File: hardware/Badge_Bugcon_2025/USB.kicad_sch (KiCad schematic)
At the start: 38 parts, among them J10 Battery, J3 USB_A, J4 USB_A, J6 USB_A, P4 USB_C_Plug_USB2.0, Q1 DMG3415U-7, SW1 ON, SW4 On, U1 USB3740B-AI9, U2 TP4056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

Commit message: feat(Hw):Update_Schematic_And_Floorplan
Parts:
- J10: footprint Footprints:Batt -> Battery:BatteryHolder_Keystone_1042_1x18650
- R31: footprint LED_SMD:LED_0603_1608Metric -> Resistor_SMD:R_0603_1608Metric
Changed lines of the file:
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@@
 			)
 		)
-		(property "Footprint" "Footprints:Batt"
+		(property "Footprint" "Battery:BatteryHolder_Keystone_1042_1x18650"
 			(at 274.32 60.96 0)
 			(effects
@@
 			)
 		)
-		(property "Footprint" "LED_SMD:LED_0603_1608Metric"
+		(property "Footprint" "Resistor_SMD:R_0603_1608Metric"
 			(at 184.912 57.15 90)
 			(effects

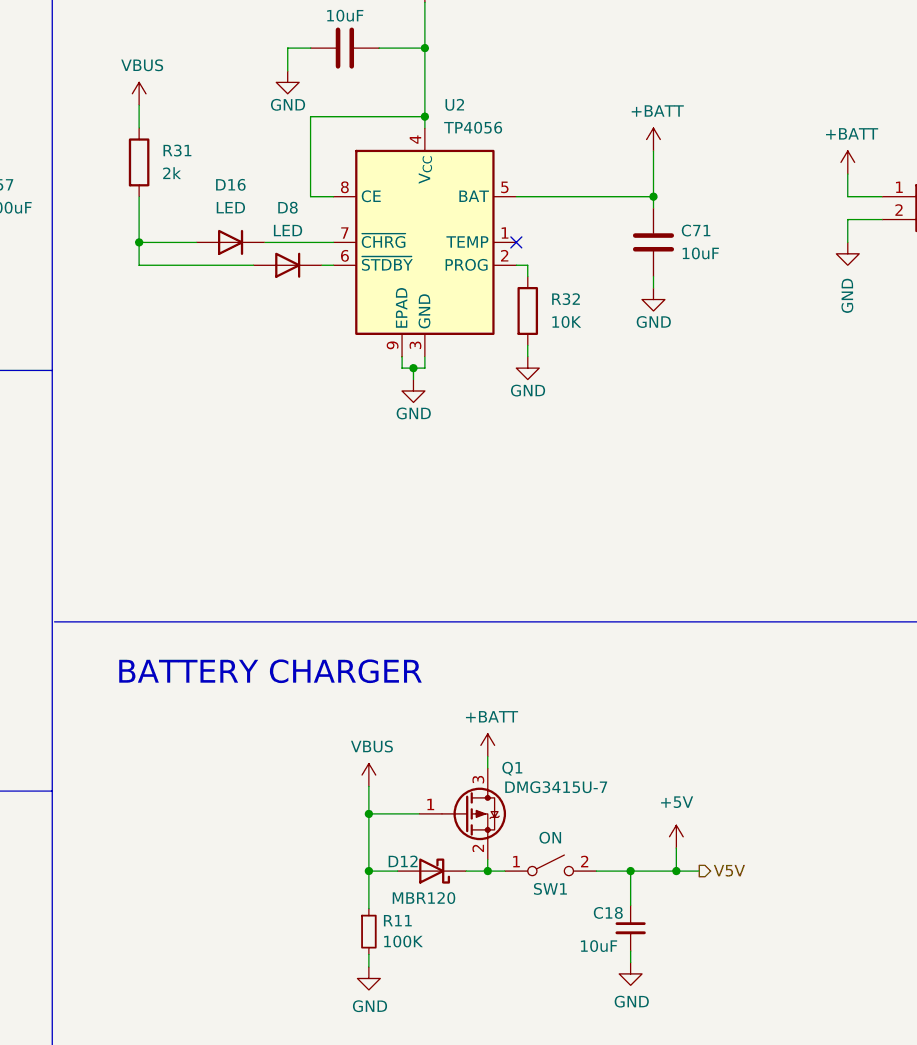
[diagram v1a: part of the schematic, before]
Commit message: feat(Hw):Update_Schematic_And_Floorplan
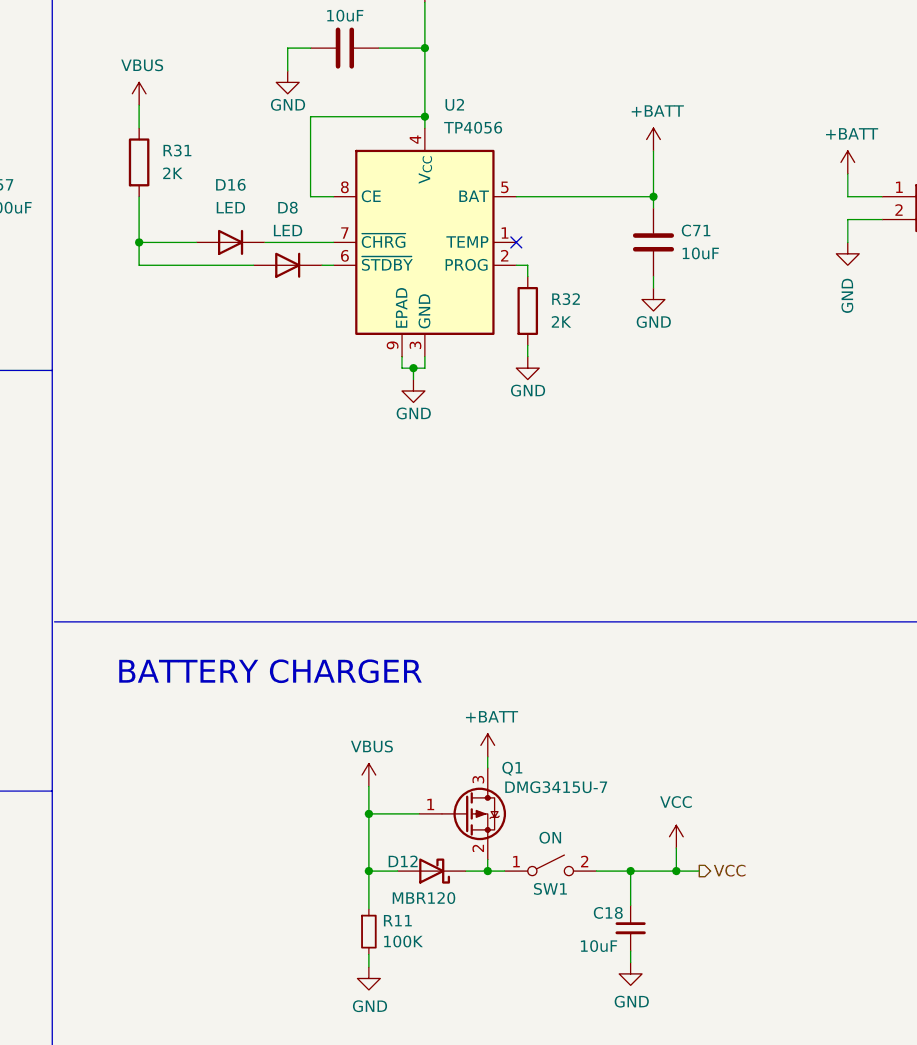
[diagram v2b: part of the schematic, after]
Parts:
- J10: footprint Battery:BatteryHolder_Keystone_1042_1x18650 -> Footprints:BatteryHolder_Keystone_1042_1x18650
- R31: value 2k -> 2K
- R32: value 10K -> 2K; footprint Resistor_SMD:R_0402_1005Metric -> Resistor_SMD:R_0603_1608Metric; LCSC# C2759535 -> C2907022
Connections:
- net +5V renamed VCC
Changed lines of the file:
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@@
 		)
 	)
-	(hierarchical_label "V5V"
+	(hierarchical_label "VCC"
 		(shape output)
 		(at 248.92 135.89 0)
@@
 			)
 		)
-		(property "Footprint" "Battery:BatteryHolder_Keystone_1042_1x18650"
+		(property "Footprint" "Footprints:BatteryHolder_Keystone_1042_1x18650"
 			(at 274.32 60.96 0)
 			(effects
@@
 	)
 	(symbol
+		(lib_id "power:VCC")
+		(at 246.38 133.35 0)
+		(unit 1)
+		(exclude_from_sim no)
+		(in_bom yes)
+		(on_board yes)
+		(dnp no)
+		(fields_autoplaced yes)
+		(property "Reference" "#PWR016"
+			(at 246.38 137.16 0)
+			(effects
+				(font
+					(size 1.27 1.27)
+				)
+				(hide yes)
+			)
+		)
+		(property "Value" "VCC"
+			(at 246.38 128.27 0)
+			(effects
+				(font
+					(size 1.27 1.27)
+				)
+			)
+		)
+		(property "Footprint" ""
+			(at 246.38 133.35 0)
+			(effects
+				(font
+					(size 1.27 1.27)
+				)
+				(hide yes)
+			)
+		)
+		(property "Datasheet" ""
+			(at 246.38 133.35 0)
+			(effects
+				(font
+					(size 1.27 1.27)
+				)
+				(hide yes)
+			)
+		)
+		(property "Description" "Power symbol creates a global label with name \"VCC\""
+			(at 246.38 133.35 0)
+			(effects
+				(font
+					(size 1.27 1.27)
+				)
+				(hide yes)
+			)
+		)
+		(pin "1"
+		)
+		(instances
+			(project ""
+				(path "/a95785a0-0aa1-454e-b59f-0ac64970ac71/a5c26cac-72fa-4752-a660-9cd751934916"
+					(reference "#PWR016")
+					(unit 1)
+				)
+			)
+		)
+	)
+	(symbol
 		(lib_id "Switch:SW_SPST")
 		(at 232.41 135.89 0)
@@
 	)
 	(symbol
-		(lib_id "power:+5V")
-		(at 246.38 133.35 0)
-		(unit 1)
-		(exclude_from_sim no)
-		(in_bom yes)
-		(on_board yes)
-		(dnp no)
-		(fields_autoplaced yes)
-		(property "Reference" "#PWR090"
-			(at 246.38 137.16 0)
-			(effects
-				(font
-					(size 1.27 1.27)
-				)
-				(hide yes)
-			)
-		)
-		(property "Value" "+5V"
-			(at 246.38 128.27 0)
-			(effects
-				(font
-					(size 1.27 1.27)
-				)
-			)
-		)
-		(property "Footprint" ""
-			(at 246.38 133.35 0)
-			(effects
-				(font
-					(size 1.27 1.27)
-				)
-				(hide yes)
-			)
-		)
-		(property "Datasheet" ""
-			(at 246.38 133.35 0)
-			(effects
-				(font
-					(size 1.27 1.27)
-				)
-				(hide yes)
-			)
-		)
-		(property "Description" "Power symbol creates a global label with name \"+5V\""
-			(at 246.38 133.35 0)
-			(effects
-				(font
-					(size 1.27 1.27)
-				)
-				(hide yes)
-			)
-		)
-		(pin "1"
-		)
-		(instances
-			(project "Badge_Bugcon_2025"
-				(path "/a95785a0-0aa1-454e-b59f-0ac64970ac71/a5c26cac-72fa-4752-a660-9cd751934916"
-					(reference "#PWR090")
-					(unit 1)
-				)
-			)
-		)
-	)
-	(symbol
 		(lib_id "power:GND")
 		(at 241.3 146.05 0)
@@
 			)
 		)
-		(property "Value" "10K"
+		(property "Value" "2K"
 			(at 232.41 74.9299 0)
 			(effects
@@
 			)
 		)
-		(property "Footprint" "Resistor_SMD:R_0402_1005Metric"
+		(property "Footprint" "Resistor_SMD:R_0603_1608Metric"
 			(at 228.092 73.66 90)
 			(effects
@@
 			)
 		)
-		(property "LCSC#" "C2759535"
+		(property "LCSC#" "C2907022"
 			(at 229.87 73.66 0)
 			(effects
@@
 			)
 		)
-		(property "Value" "2k"
+		(property "Value" "2K"
 			(at 189.23 58.4199 0)
 			(effects

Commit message: feat(Hw):Update_Floorplan
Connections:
- net 1_DM: now also J3.2 (D-), U3.9 (UDM); no longer P4.A7 (D-)
- net 1_DP: now also J3.3 (D+), U3.10 (UDP); no longer P4.A6 (D+)
- net 2_DM: now also P4.A7 (D-); no longer J3.2 (D-), U3.9 (UDM)
- net 2_DP: now also P4.A6 (D+); no longer J3.3 (D+), U3.10 (UDP)
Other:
- moved on the sheet: C19, C55, C56, C57, D13, D14, D15, D2, F1, F2, F3, F4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

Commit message: feat(Hw):Init_Route
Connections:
- net 1_DM renamed 1_DN
- net 2_DM renamed 2_DN
- net 3_DM renamed 3_DN
- net 4_DM renamed 4_DN
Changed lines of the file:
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@@
 		)
 	)
-	(label "4_DM"
+	(label "4_DN"
 		(at 140.97 179.07 180)
 		(effects
@@
 		)
 	)
-	(label "2_DM"
+	(label "2_DN"
 		(at 72.39 101.6 180)
 		(effects
@@
 		)
 	)
-	(label "1_DM"
+	(label "1_DN"
 		(at 31.75 160.02 0)
 		(effects
@@
 		)
 	)
-	(label "2_DM"
+	(label "2_DN"
 		(at 62.23 43.18 0)
 		(effects
@@
 		)
 	)
-	(label "3_DM"
+	(label "3_DN"
 		(at 107.95 156.21 0)
 		(effects
@@
 		)
 	)
-	(label "1_DM"
+	(label "1_DN"
 		(at 72.39 109.22 180)
 		(effects
@@
 		)
 	)
-	(label "4_DM"
+	(label "4_DN"
 		(at 107.95 161.29 0)
 		(effects
@@
 		)
 	)
-	(label "1_DM"
+	(label "1_DN"
 		(at 82.55 153.67 180)
 		(effects
@@
 		)
 	)
-	(label "3_DM"
+	(label "3_DN"
 		(at 140.97 146.05 180)
 		(effects

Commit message: feat(Hw):Update_BOM_And_Labels
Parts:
- R14, R15: LCSC# C191782 -> C2907044
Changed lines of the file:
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@@
 			)
 		)
-		(property "LCSC#" "C191782"
+		(property "LCSC#" "C2907044"
 			(at 66.04 35.56 0)
 			(effects
@@
 			)
 		)
-		(property "LCSC#" "C191782"
+		(property "LCSC#" "C2907044"
 			(at 66.04 38.1 0)
 			(effects

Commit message: feat(Hw):Update_Route
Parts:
- J3, J4, J6: footprint Connector_USB:USB_A_Connfly_DS1095 -> Footprints:USB_A_Connfly_DS1095; LCSC# C18077686 -> C2345
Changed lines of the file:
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@@
 			)
 		)
-		(property "Footprint" "Connector_USB:USB_A_Connfly_DS1095"
+		(property "Footprint" "Footprints:USB_A_Connfly_DS1095"
 			(at 25.4 158.75 0)
 			(effects
@@
 			)
 		)
-		(property "LCSC#" "C18077686"
+		(property "LCSC#" "C2345"
 			(at 21.59 157.48 0)
 			(effects
@@
 			)
 		)
-		(property "Footprint" "Connector_USB:USB_A_Connfly_DS1095"
+		(property "Footprint" "Footprints:USB_A_Connfly_DS1095"
 			(at 146.05 144.78 0)
 			(effects
@@
 			)
 		)
-		(property "LCSC#" "C18077686"
+		(property "LCSC#" "C2345"
 			(at 149.86 143.51 0)
 			(effects
@@
 			)
 		)
-		(property "Footprint" "Connector_USB:USB_A_Connfly_DS1095"
+		(property "Footprint" "Footprints:USB_A_Connfly_DS1095"
 			(at 146.05 177.8 0)
 			(effects
@@
 			)
 		)
-		(property "LCSC#" "C18077686"
+		(property "LCSC#" "C2345"
 			(at 149.86 176.53 0)
 			(effects

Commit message: feat(Hw):Update_Schematic
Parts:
- removed D13: 1N5817, Diode_SMD:D_SOD-123F, symbol Diode:1N5817
- removed F2: 750mA, Fuse:Fuse_0603_1608Metric, symbol Device:Fuse_Small
- removed J3: USB_A, Footprints:USB_A_Connfly_DS1095, symbol Connector:USB_A
- added C21, C22: 22uF, symbol Device:C
- added D9: D, symbol Device:D
- added L1: 4.7uH, symbol Device:L
- added R37: 110K, symbol Device:R
- added R40: 15K, symbol Device:R
- added U4: MT3608, Package_TO_SOT_SMD:SOT-23-6, symbol Regulator_Switching:MT3608
- added U5: AP2112K-3.3, Package_TO_SOT_SMD:SOT-23-5, symbol Regulator_Linear:AP2112K-3.3
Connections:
- net GND: now also C21.2, C22.2, R40.2
- new net: C22.1, L1.1, U4.5 (IN)
- new net: D9.2 (A), L1.2, U4.1 (SW)
- new net: C21.1, D9.1 (K), R37.1
- new net: R37.2, R40.1, U4.3 (FB)
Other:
- note added: "HUB"
- note added: "VOLTAGE SELECTOR"
- note removed: "USB-A"
- moved on the sheet: C18, C19, C55, C56, C57, D12, D14, D15, F3, F4, J4, J6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

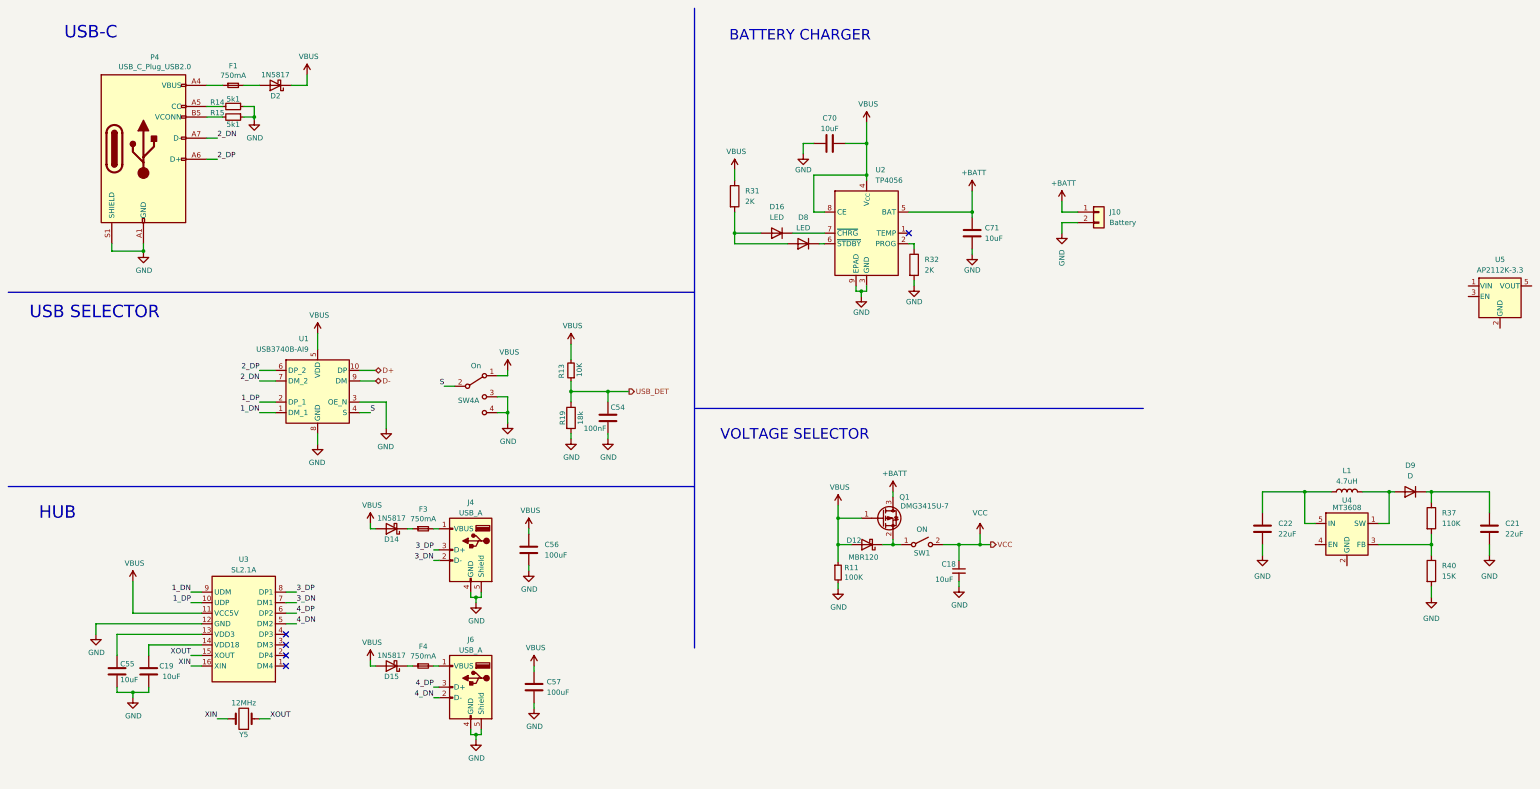
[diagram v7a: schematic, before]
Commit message: feat(Hw):Update_Schaematic_And_BOM
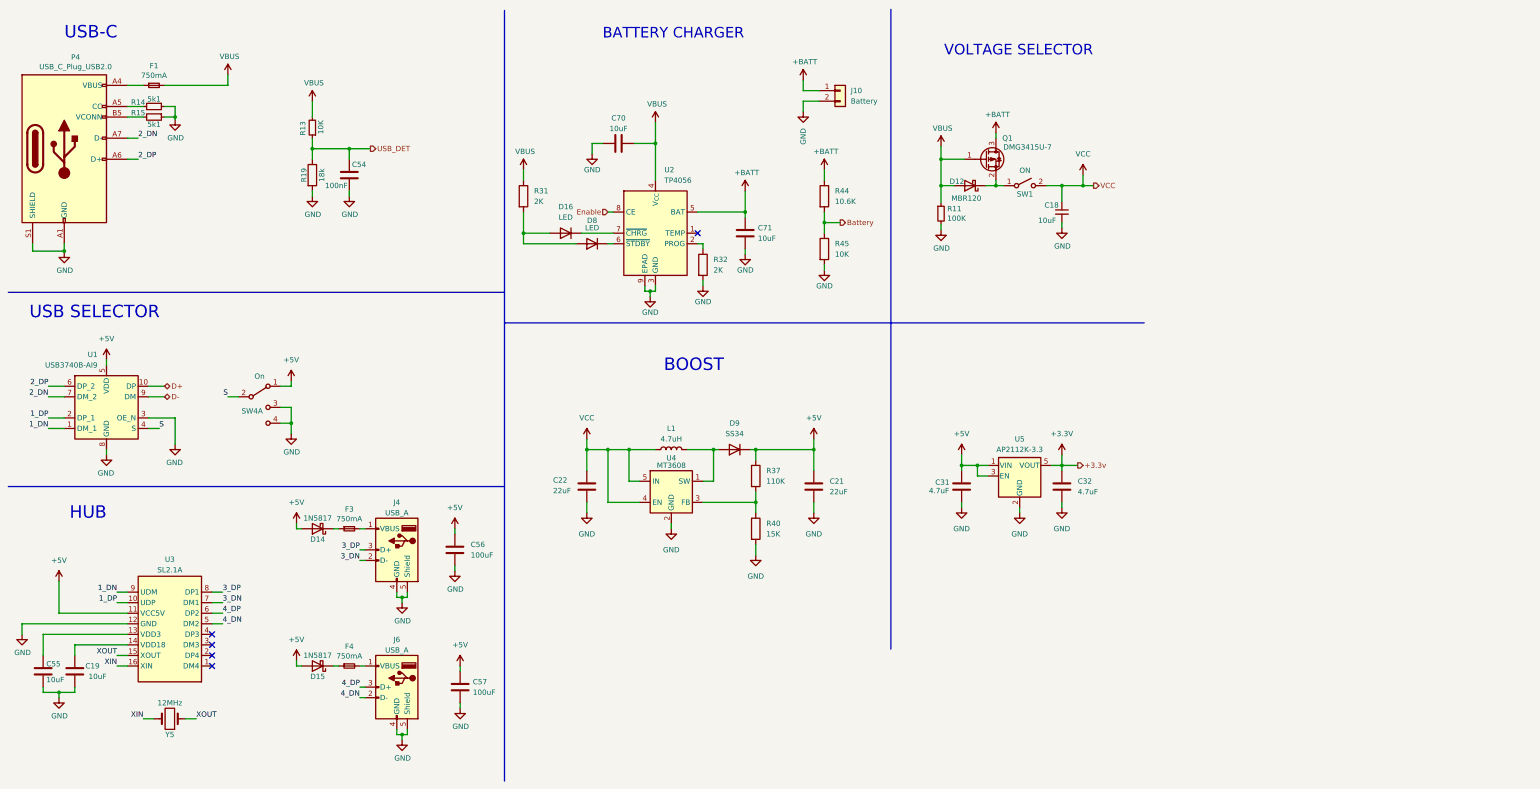
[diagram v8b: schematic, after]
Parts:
- removed D2: 1N5817, Diode_SMD:D_SOD-123F, symbol Diode:1N5817
- added C31, C32: 4.7uF, symbol Device:C
- added R44: 10.6K, symbol Device:R
- added R45: 10K, symbol Device:R
- D9: value D -> SS34; LCSC# (none) -> C908680
- L1: LCSC# (none) -> C520334
- R37: footprint (none) -> Resistor_SMD:R_0603_1608Metric; LCSC# (none) -> C326736
- R40: footprint (none) -> Resistor_SMD:R_0603_1608Metric; LCSC# (none) -> C2989599
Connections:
- net +BATT: now also R44.1
- net GND: now also U4.2 (GND), U5.2 (GND), C31.2, C32.2, R45.2
- net VBUS: now also F1.2; no longer C56.1, C57.1, D14.2 (A), D15.2 (A), SW4.1 (A), U1.5 (VDD), U2.8 (CE), U3.11 (VCC5V)
- net VCC: now also C22.1, L1.1, U4.4 (EN), U4.5 (IN)
- net +5V: now reaches C21.1, D9.1 (K), R37.1
- net +5V: now also C56.1, C57.1, D14.2 (A), D15.2 (A), SW4.1 (A), U1.5 (VDD), U3.11 (VCC5V), U5.1 (VIN), U5.3 (EN), C31.1
- net +3.3V: now reaches U5.5 (VOUT)
- net +3.3V: now also C32.1
- new net Battery: R44.2, R45.1
- new net Enable: U2.8 (CE)
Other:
- note added: "BOOST"
- moved on the sheet: C18, C19, C21, C22, C54, C55, C56, C57, C70, C71, D12, D14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
